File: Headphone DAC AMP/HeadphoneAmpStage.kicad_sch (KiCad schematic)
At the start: 48 parts, among them U3 TPA6120A2DWP, U4 OPA1612AxD, U5 OPA1612AxD

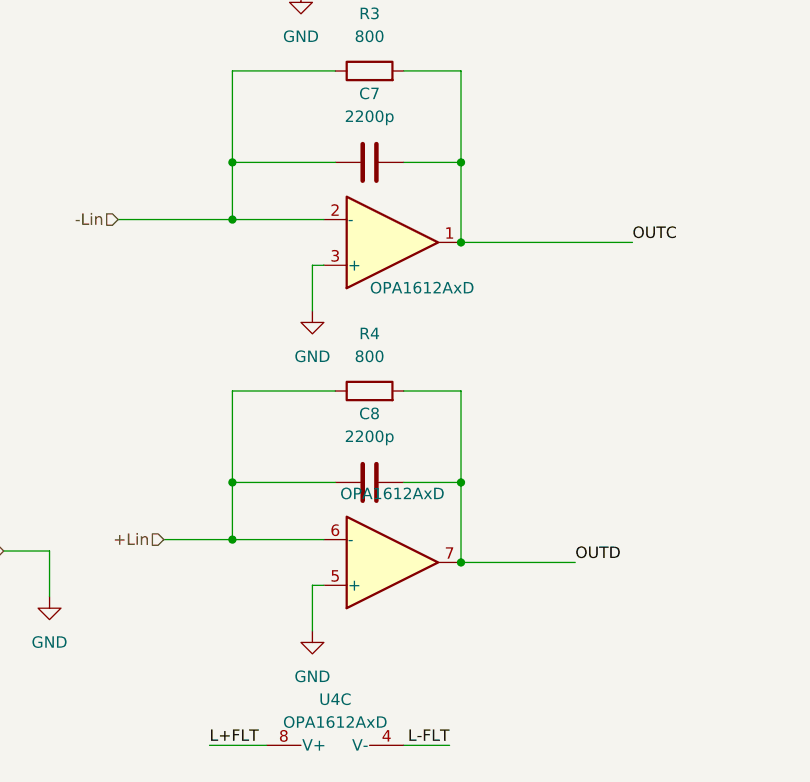
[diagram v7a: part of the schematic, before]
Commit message: Swapped to 0603 caps in order to compact design
Planning on a 100x70mm board shape
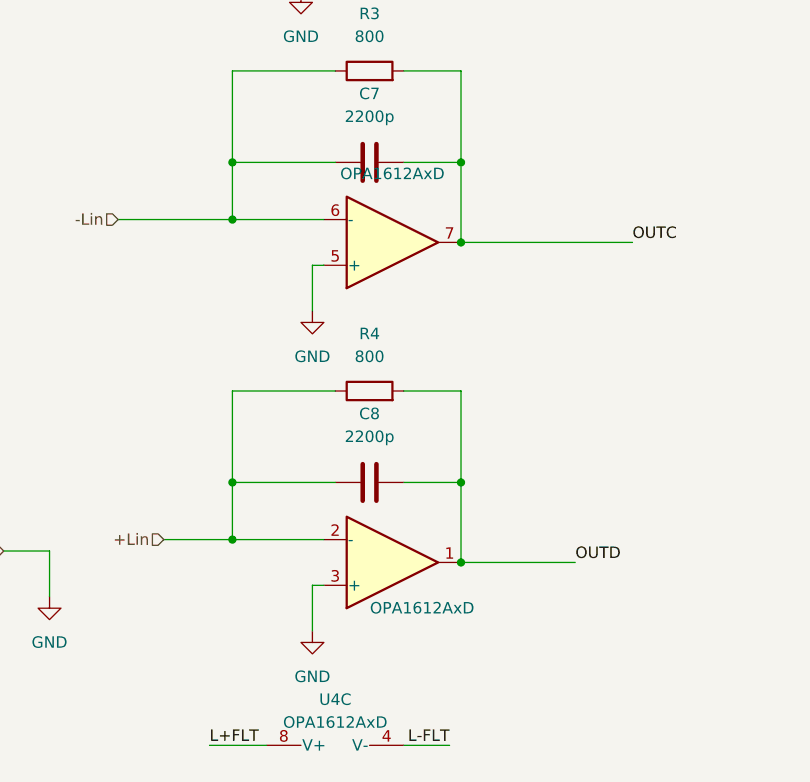
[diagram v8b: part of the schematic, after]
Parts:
- C5, C6, C65, C66, C7, C71, C72, C76, C77, C8, C81, C82: footprint Capacitor_SMD:C_0805_2012Metric_Pad1.18x1.45mm_HandSolder -> Capacitor_SMD:C_0603_1608Metric_Pad1.08x0.95mm_HandSolder
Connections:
- net +Lin: now also U5.2 (-); no longer U5.6 (-)
- net -Lin: now also U5.6 (-); no longer U5.2 (-)
- net OUTC: now also U5.7; no longer U5.1
- net OUTD: now also U5.1; no longer U5.7
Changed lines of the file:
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@@
 	)
 	(junction
+		(at 74.93 148.59)
+		(diameter 0)
+		(color 0 0 0 0)
+	)
+	(junction
 		(at 154.94 111.76)
 		(diameter 0)
@@
 	)
 	(junction
-		(at 74.93 113.03)
-		(diameter 0)
-		(color 0 0 0 0)
-	)
-	(junction
 		(at 257.81 143.51)
 		(diameter 0)
@@
 	)
 	(junction
-		(at 74.93 148.59)
-		(diameter 0)
-		(color 0 0 0 0)
-	)
-	(junction
 		(at 257.81 119.38)
 		(diameter 0)
@@
 	)
 	(junction
+		(at 74.93 113.03)
+		(diameter 0)
+		(color 0 0 0 0)
+	)
+	(junction
 		(at 234.95 111.76)
 		(diameter 0)
@@
 			)
 		)
-		(property "Footprint" "Capacitor_SMD:C_0805_2012Metric_Pad1.18x1.45mm_HandSolder"
+		(property "Footprint" "Capacitor_SMD:C_0603_1608Metric_Pad1.08x0.95mm_HandSolder"
 			(at 258.7752 151.13 0)
 			(effects
@@
 			)
 		)
-		(property "Footprint" "Capacitor_SMD:C_0805_2012Metric_Pad1.18x1.45mm_HandSolder"
+		(property "Footprint" "Capacitor_SMD:C_0603_1608Metric_Pad1.08x0.95mm_HandSolder"
 			(at 68.58 138.7348 0)
 			(effects
@@
 			)
 		)
-		(property "Footprint" "Capacitor_SMD:C_0805_2012Metric_Pad1.18x1.45mm_HandSolder"
+		(property "Footprint" "Capacitor_SMD:C_0603_1608Metric_Pad1.08x0.95mm_HandSolder"
 			(at 68.58 103.1748 0)
 			(effects
@@
 			)
 		)
-		(property "Footprint" "Capacitor_SMD:C_0805_2012Metric_Pad1.18x1.45mm_HandSolder"
+		(property "Footprint" "Capacitor_SMD:C_0603_1608Metric_Pad1.08x0.95mm_HandSolder"
 			(at 268.9352 135.89 0)
 			(effects
@@
 	(symbol
 		(lib_id "Amplifier_Operational:OPA1612AxD")
-		(at 67.31 113.03 0)
+		(at 67.31 148.59 0)
 		(mirror x)
 		(unit 1)
@@
 		(dnp no)
 		(property "Reference" "U5"
-			(at 67.31 123.19 0)
+			(at 67.31 158.75 0)
 			(effects
 				(font
@@
 		)
 		(property "Value" "OPA1612AxD"
-			(at 70.612 118.11 0)
+			(at 70.612 153.67 0)
 			(effects
 				(font
@@
 		)
 		(property "Footprint" "Package_SO:SOIC-8-1EP_3.9x4.9mm_P1.27mm_EP2.95x4.9mm_Mask2.71x3.4mm_ThermalVias"
-			(at 67.31 113.03 0)
+			(at 67.31 148.59 0)
 			(effects
 				(font
@@
 		)
 		(property "Datasheet" "http://www.ti.com/lit/ds/symlink/opa1612.pdf"
-			(at 67.31 113.03 0)
+			(at 67.31 148.59 0)
 			(effects
 				(font
@@
 		)
 		(property "Description" "Dual SoundPlus High Performance, Bipolar-Input Audio Operational Amplifiers, SOIC-8"
-			(at 67.31 113.03 0)
+			(at 67.31 148.59 0)
 			(effects
 				(font
@@
 	(symbol
 		(lib_id "Amplifier_Operational:OPA1612AxD")
-		(at 67.31 148.59 0)
+		(at 67.31 113.03 0)
 		(mirror x)
 		(unit 2)
@@
 		(fields_autoplaced yes)
 		(property "Reference" "U5"
-			(at 67.31 158.75 0)
+			(at 67.31 123.19 0)
 			(effects
 				(font
@@
 		)
 		(property "Value" "OPA1612AxD"
-			(at 67.31 140.97 0)
+			(at 67.31 105.41 0)
 			(effects
 				(font
@@
 		)
 		(property "Footprint" "Package_SO:SOIC-8-1EP_3.9x4.9mm_P1.27mm_EP2.95x4.9mm_Mask2.71x3.4mm_ThermalVias"
-			(at 67.31 148.59 0)
+			(at 67.31 113.03 0)
 			(effects
 				(font
@@
 		)
 		(property "Datasheet" "http://www.ti.com/lit/ds/symlink/opa1612.pdf"
-			(at 67.31 148.59 0)
+			(at 67.31 113.03 0)
 			(effects
 				(font
@@
 		)
 		(property "Description" "Dual SoundPlus High Performance, Bipolar-Input Audio Operational Amplifiers, SOIC-8"
-			(at 67.31 148.59 0)
+			(at 67.31 113.03 0)
 			(effects
 				(font
@@
 			)
 		)
-		(property "Footprint" "Capacitor_SMD:C_0805_2012Metric_Pad1.18x1.45mm_HandSolder"
+		(property "Footprint" "Capacitor_SMD:C_0603_1608Metric_Pad1.08x0.95mm_HandSolder"
 			(at 67.31 30.7848 0)
 			(effects
@@
 			)
 		)
-		(property "Footprint" "Capacitor_SMD:C_0805_2012Metric_Pad1.18x1.45mm_HandSolder"
+		(property "Footprint" "Capacitor_SMD:C_0603_1608Metric_Pad1.08x0.95mm_HandSolder"
 			(at 268.9352 104.14 0)
 			(effects
@@
 			)
 		)
-		(property "Footprint" "Capacitor_SMD:C_0805_2012Metric_Pad1.18x1.45mm_HandSolder"
+		(property "Footprint" "Capacitor_SMD:C_0603_1608Metric_Pad1.08x0.95mm_HandSolder"
 			(at 258.7752 119.38 0)
 			(effects
@@
 			)
 		)
-		(property "Footprint" "Capacitor_SMD:C_0805_2012Metric_Pad1.18x1.45mm_HandSolder"
+		(property "Footprint" "Capacitor_SMD:C_0603_1608Metric_Pad1.08x0.95mm_HandSolder"
 			(at 268.9352 119.38 0)
 			(effects
@@
 			)
 		)
-		(property "Footprint" "Capacitor_SMD:C_0805_2012Metric_Pad1.18x1.45mm_HandSolder"
+		(property "Footprint" "Capacitor_SMD:C_0603_1608Metric_Pad1.08x0.95mm_HandSolder"
 			(at 258.7752 135.89 0)
 			(effects
@@
 			)
 		)
-		(property "Footprint" "Capacitor_SMD:C_0805_2012Metric_Pad1.18x1.45mm_HandSolder"
+		(property "Footprint" "Capacitor_SMD:C_0603_1608Metric_Pad1.08x0.95mm_HandSolder"
 			(at 67.31 67.6148 0)
 			(effects
@@
 			)
 		)
-		(property "Footprint" "Capacitor_SMD:C_0805_2012Metric_Pad1.18x1.45mm_HandSolder"
+		(property "Footprint" "Capacitor_SMD:C_0603_1608Metric_Pad1.08x0.95mm_HandSolder"
 			(at 258.7752 104.14 0)
 			(effects
@@
 			)
 		)
-		(property "Footprint" "Capacitor_SMD:C_0805_2012Metric_Pad1.18x1.45mm_HandSolder"
+		(property "Footprint" "Capacitor_SMD:C_0603_1608Metric_Pad1.08x0.95mm_HandSolder"
 			(at 268.9352 151.13 0)
 			(effects
